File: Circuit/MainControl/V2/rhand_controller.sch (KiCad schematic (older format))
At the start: 18 parts, among them P1 BLUETOOTH, SW1 EmSW, SW2 SWITCH_INV, U1 IM315TRX, U2 STM32F042

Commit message: ラベル名のつけ方変更
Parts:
- SW1: footprint YASU:XA_2Pin -> YASU:XA_2Pin_LP
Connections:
- net +3V3: now also S1.8; no longer S1.5
- net DSW_B0: now also S1.1; no longer S1.2
- net DSW_B1: now also S1.2; no longer S1.3
- net DSW_B2: now also S1.3; no longer S1.4
- net Move_X: now also U2.7 (PA1/USART2_RTS/TIM2_CH2/TSC_G1_IO2/EVENTOUT/ADC_IN1); no longer U2.6 (PA0/USART2_CTS/TIM2_CH1_ETR/TSC_G1_IO1/ADC_IN0)
- net Move_Y: now also U2.6 (PA0/USART2_CTS/TIM2_CH1_ETR/TSC_G1_IO1/ADC_IN0); no longer U2.7 (PA1/USART2_RTS/TIM2_CH2/TSC_G1_IO2/EVENTOUT/ADC_IN1)
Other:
- moved on the sheet: S1
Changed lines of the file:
@@
 Wire Wire Line
 	10000 5000 10450 5000
+Text Label 2850 4700 0    60   ~ 0
+Move_Y
 Text Label 2850 4800 0    60   ~ 0
-Move_Y
-Text Label 2850 4700 0    60   ~ 0
 Move_X
 Wire Wire Line
@@
 F 0 "SW1" H 8650 3660 50  0000 C CNN
 F 1 "EmSW" H 8500 3470 50  0000 C CNN
-F 2 "YASU:XA_2Pin" H 8500 3550 50  0001 C CNN
+F 2 "YASU:XA_2Pin_LP" H 8500 3550 50  0001 C CNN
 F 3 "" H 8500 3550 50  0000 C CNN
 	1    8500 3550
@@
 L SW_DIP_x4 S1
 U 1 1 593A8DBA
-P 1050 5750
-F 0 "S1" H 1050 5500 50  0000 C CNN
-F 1 "SW_DIP_x4" H 1050 6000 50  0000 C CNN
-F 2 "Buttons_Switches_THT:SW_DIP_x4_W7.62mm_Slide" H 1000 5750 50  0001 C CNN
-F 3 "" H 1000 5750 50  0000 C CNN
-	1    1050 5750
+P 1050 5850
+F 0 "S1" H 1050 5600 50  0000 C CNN
+F 1 "SW_DIP_x4" H 1050 6100 50  0000 C CNN
+F 2 "Buttons_Switches_THT:SW_DIP_x4_W7.62mm_Slide" H 1000 5850 50  0001 C CNN
+F 3 "" H 1000 5850 50  0000 C CNN
+	1    1050 5850
 	-1   0    0    -1
 $EndComp
@@
 Connection ~ 2050 5800
 Connection ~ 2200 5700
-NoConn ~ 1350 5600
-NoConn ~ 750  5600
+NoConn ~ 1350 6000
+NoConn ~ 750  6000
 Wire Wire Line
 	700  5900 750  5900
@@
 F0 "RHand" 60
 F1 "Right_hand.sch" 60
-F2 "Joy_X" O R 2400 4700 60
-F3 "Joy_Y" O R 2400 4800 60
+F2 "Joy_X" O R 2400 4800 60
+F3 "Joy_Y" O R 2400 4700 60
 F4 "SW" O L 1700 4800 60
 $EndSheet

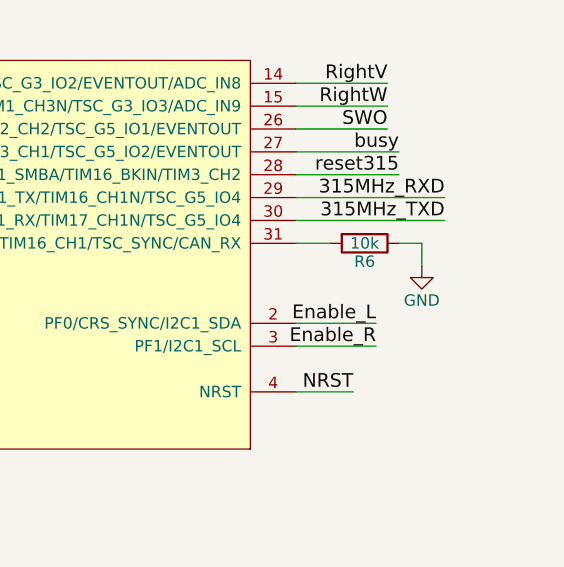
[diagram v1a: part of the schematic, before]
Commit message: 配線が半分完了,電源と無線モジュールが未配線
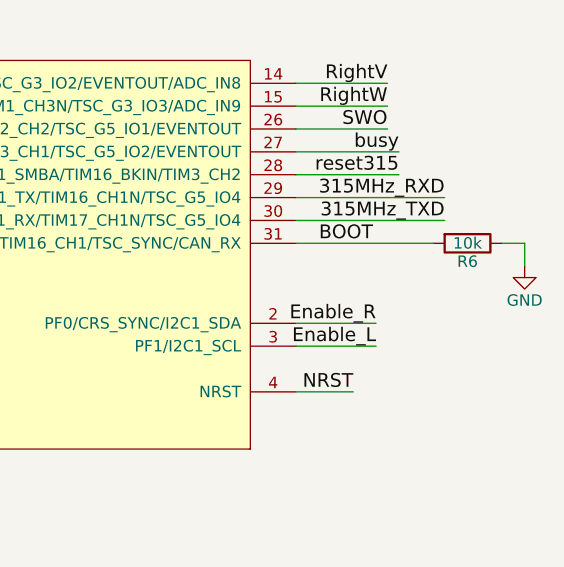
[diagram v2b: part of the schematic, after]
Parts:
- U1: footprint YASU:Pin_Header_Straight_2x13_Pitch1.27mm_SMD_foIM315 -> YASU:IM315
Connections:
- net Enable_L: now also U2.3 (PF1/I2C1_SCL); no longer U2.2 (PF0/CRS_SYNC/I2C1_SDA)
- net Enable_R: now also U2.2 (PF0/CRS_SYNC/I2C1_SDA); no longer U2.3 (PF1/I2C1_SCL)
- net BOOT: now reaches R6.2, U2.31 (PB8/BOOT0/I2C1_SCL/CEC/TIM16_CH1/TSC_SYNC/CAN_RX)
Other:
- moved on the sheet: R6
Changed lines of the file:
@@
 L GND #PWR04
 U 1 1 5936E290
-P 10550 5500
-F 0 "#PWR04" H 10550 5250 50  0001 C CNN
-F 1 "GND" H 10550 5350 50  0000 C CNN
-F 2 "" H 10550 5500 50  0000 C CNN
-F 3 "" H 10550 5500 50  0000 C CNN
-	1    10550 5500
+P 11000 5500
+F 0 "#PWR04" H 11000 5250 50  0001 C CNN
+F 1 "GND" H 11000 5350 50  0000 C CNN
+F 2 "" H 11000 5500 50  0000 C CNN
+F 3 "" H 11000 5500 50  0000 C CNN
+	1    11000 5500
 	1    0    0    -1
 $EndComp
@@
 L R R6
 U 1 1 5936E3FC
-P 10300 5400
-F 0 "R6" V 10380 5400 50  0000 C CNN
-F 1 "10k" V 10300 5400 50  0000 C CNN
-F 2 "YASU:R_0603_HandSoldering_LP" V 10230 5400 50  0001 C CNN
-F 3 "" H 10300 5400 50  0000 C CNN
-	1    10300 5400
+P 10750 5400
+F 0 "R6" V 10830 5400 50  0000 C CNN
+F 1 "10k" V 10750 5400 50  0000 C CNN
+F 2 "YASU:R_0603_HandSoldering_LP" V 10680 5400 50  0001 C CNN
+F 3 "" H 10750 5400 50  0000 C CNN
+	1    10750 5400
 	0    1    1    0
 $EndComp
@@
 	7200 1150 6850 1150
 Wire Wire Line
-	10150 5400 10000 5400
-Wire Wire Line
-	10550 5500 10550 5400
-Wire Wire Line
-	10550 5400 10450 5400
+	10600 5400 10000 5400
+Wire Wire Line
+	11000 5500 11000 5400
+Wire Wire Line
+	11000 5400 10900 5400
 Wire Wire Line
 	10250 6050 10000 6050
@@
 NoConn ~ 10200 2300
 Wire Wire Line
+	10000 5850 10350 5850
+Wire Wire Line
 	10000 5750 10350 5750
-Wire Wire Line
-	10000 5850 10350 5850
-Text Label 10350 5850 2    60   ~ 0
+Text Label 10350 5750 2    60   ~ 0
 Enable_R
 Wire Wire Line
@@
 F 0 "U1" H 1850 3300 60  0000 C CNN
 F 1 "IM315TRX" H 2550 3300 60  0000 C CNN
-F 2 "YASU:Pin_Header_Straight_2x13_Pitch1.27mm_SMD_foIM315" H 1775 3175 60  0001 C CNN
+F 2 "YASU:IM315" H 1775 3175 60  0001 C CNN
 F 3 "" H 1775 3175 60  0001 C CNN
 	1    2200 2400
@@
 Wire Wire Line
 	2650 5200 2650 5000
-Text Label 10350 5750 2    60   ~ 0
+Text Label 10350 5850 2    60   ~ 0
 Enable_L
 Text Label 1200 4800 0    60   ~ 0
@@
 Wire Wire Line
 	1700 5300 1200 5300
+Text Label 10100 5400 0    60   ~ 0
+BOOT
 $EndSCHEMATC
